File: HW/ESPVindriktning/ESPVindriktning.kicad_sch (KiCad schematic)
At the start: 60 parts, among them SW101 reset, SW102 boot, T101 BSS138, T102 BSS138, X101 USB_C, X102 I2C, X105 Fan, X106 PM1006, X107 I2C, X108 I2C

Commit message: Implement review findings
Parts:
- added C102: 1n, Capacitor_SMD:C_0603_1608Metric, symbol Device:C_Small
- added R103 (x2): 100R, Resistor_SMD:R_0603_1608Metric, symbol Device:R_Small
- C102: Partnumber 133-5641 -> (none); Supplier RS-Components -> (none)
- C221, C222, C224, C225, C501, C502, R101, R102, R103, R223: Supplier RS-Components -> (none)
- PD101: value PT26-51B/TR8 -> SFH 3716; footprint LED_SMD:LED_1210_3225Metric_Pad1.42x2.65mm_HandSolder -> LED_SMD:LED_0805_2012Metric_Pad1.15x1.40mm_HandSolder; Partnumber (none) -> 720-SFH3716; Supplier (none) -> Mouser
- R103: value 4.7k -> 470R; Partnumber 595-TLV76133DCYR -> (none); Supplier Mouser -> (none)
- X102: value I2C -> WS2812
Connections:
- net +3.3V: no longer C502.1, C502.1, C502.1, C502.1, D105.1 (VDD), D106.1 (VDD), D107.1 (VDD), X102.1 (Pin_1)
- net +5V: now also C502.1, C502.1, C502.1, C502.1, D105.1 (VDD), D106.1 (VDD), D107.1 (VDD), X102.1 (Pin_1)
- net BUZZER: now also S102.17 (GPIO1/ADC1_CH1/XTAL_32K_N); no longer S102.7 (GPIO8)
- net FAN: now also S102.18 (GPIO0/ADC1_CH0/XTAL_32K_P); no longer S102.6 (GPIO7)
- net GND: now also C102.2
- net GPIO0: now also R103.1; no longer D104.2 (A2), SW102.2
- net I2C_SCL: now also S102.6 (GPIO7); no longer S102.18 (GPIO0/ADC1_CH0/XTAL_32K_P)
- net I2C_SDA: now also S102.7 (GPIO8); no longer S102.17 (GPIO1/ADC1_CH1/XTAL_32K_N)
- net USB_D+: now also S102.14 (GPIO19/USB_D+); no longer S102.13 (GPIO18/USB_D-)
- net USB_D-: now also S102.13 (GPIO18/USB_D-); no longer S102.14 (GPIO19/USB_D+)
- net ~{RESET}: now also R103.1; no longer C102.1, D102.2 (A2), SW101.2
- new net: C102.1, D102.2 (A2), R103.2, SW101.2
- new net: C102.1, D104.2 (A2), R103.2, SW102.2
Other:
- moved on the sheet: C102, D102, D104, R103, SW101, SW102

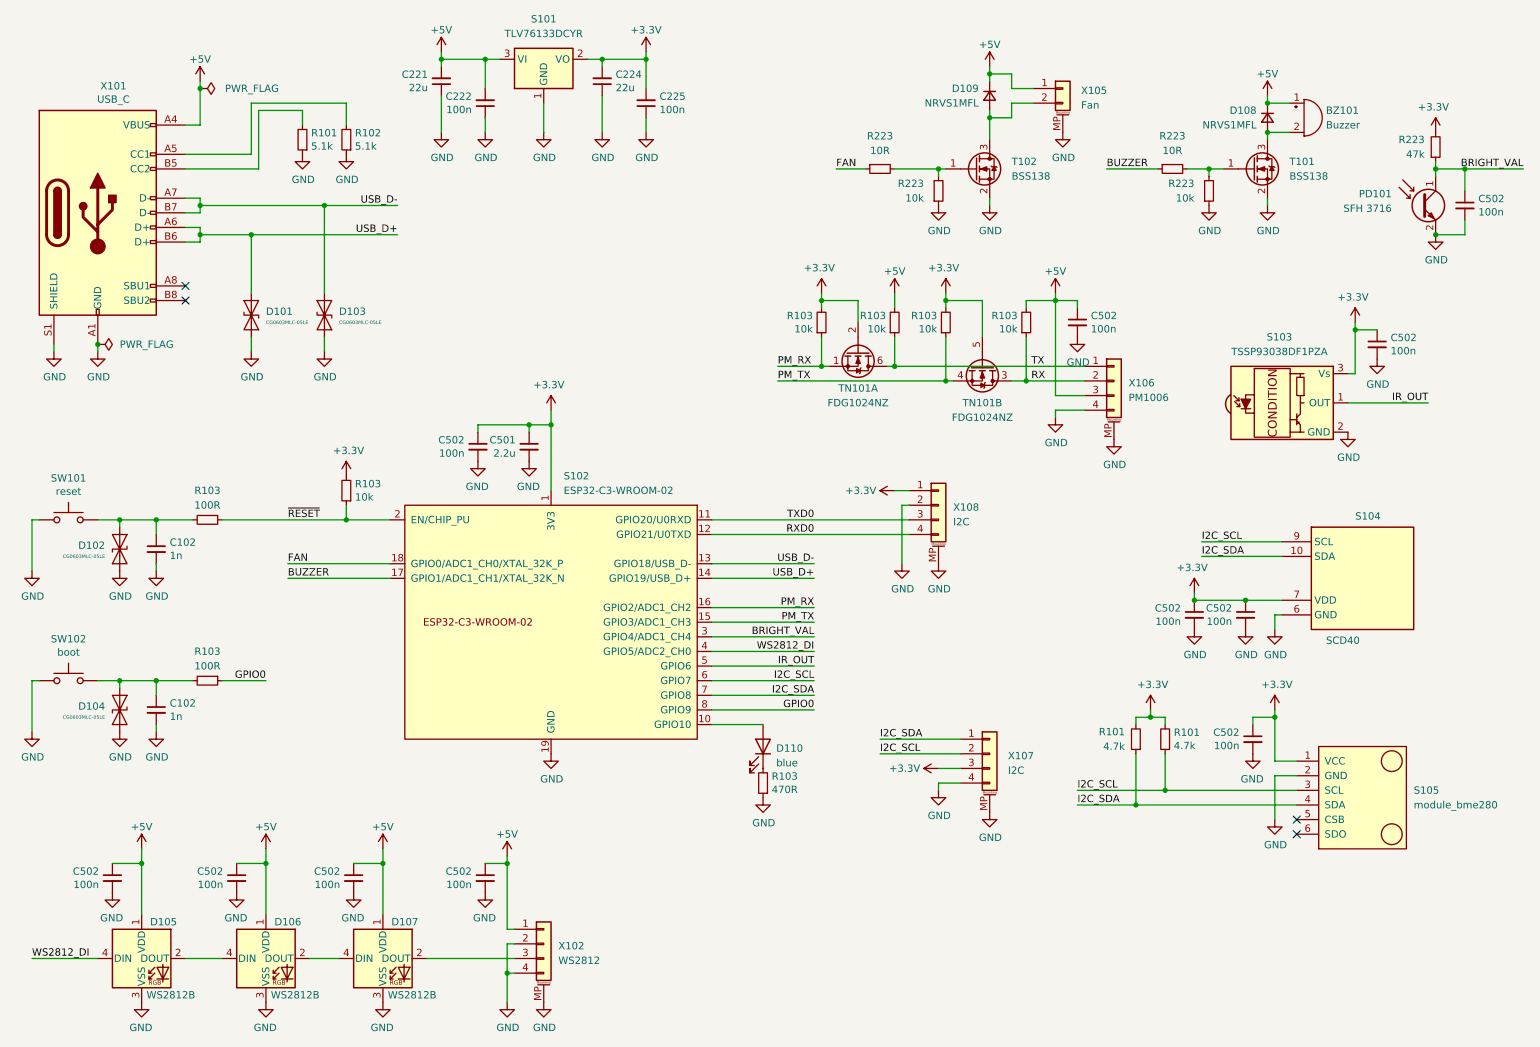
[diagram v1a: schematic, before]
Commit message: Review and layout optimization
Changes to schematic:
 - Add BME280 as ASIC under the module
 - Reduce I2C Pull-Ups to 1.2k

Changes to layout:
 - Optimize parts placement
 - Make USB approx. 9ß OHm impedance
 - General routing improvements
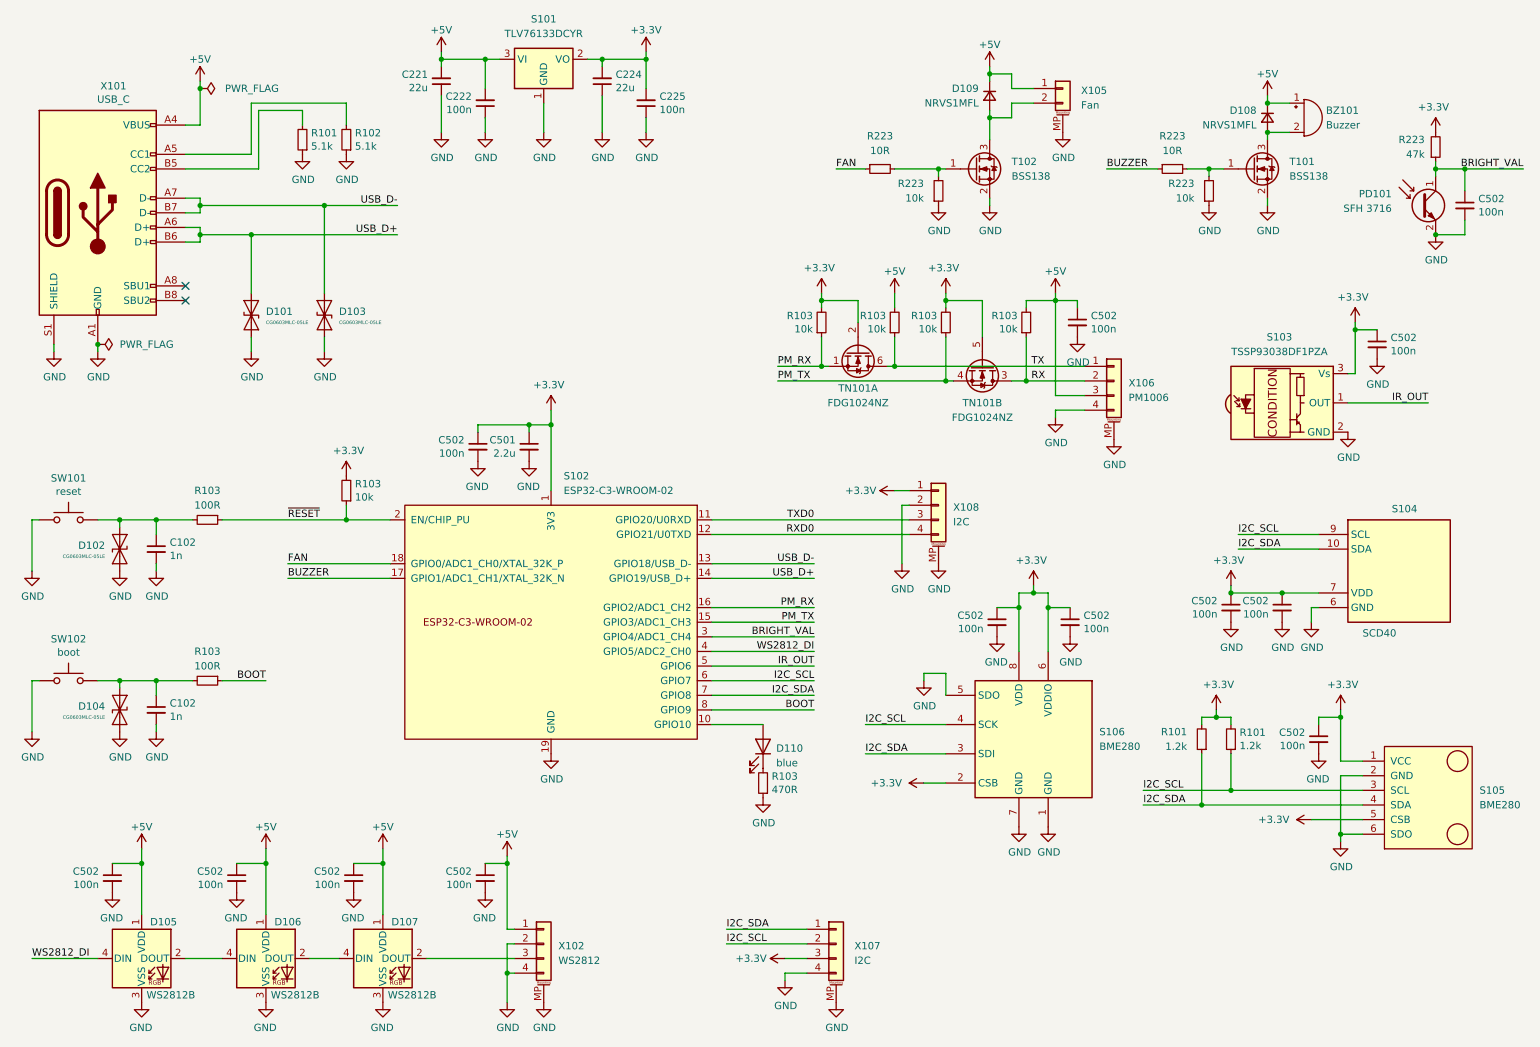
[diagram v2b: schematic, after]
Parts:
- added C502 (x2): 100n, Capacitor_SMD:C_0603_1608Metric, symbol Device:C_Small
- added S106: BME280, Package_LGA:Bosch_LGA-8_2.5x2.5mm_P0.65mm_ClockwisePinNumbering, symbol Sensor:BME280
- R101: value 4.7k -> 1.2k
- S105: value module_bme280 -> BME280
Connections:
- net +3.3V: now also S105.5 (CSB), C502.1, C502.1, S106.2 (CSB), S106.6 (VDDIO), S106.8 (VDD)
- net GND: now also S105.6 (SDO), C502.2, C502.2, S106.1 (GND), S106.5 (SDO), S106.7 (GND)
- net I2C_SCL: now also S106.4 (SCK)
- net I2C_SDA: now also S106.3 (SDI)
- net GPIO0 renamed BOOT
- no-connect marks 4 -> 2
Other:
- moved on the sheet: C502, R101, S104, S105, X107

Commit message: ESP32-C3 pinout change
Change pinout due to GPIO2 needing a Pull-Up (strapping pin)
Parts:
- added R103: 10k, Resistor_SMD:R_0603_1608Metric, symbol Device:R_Small
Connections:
- net +3.3V: now also R103.2
- net BRIGHT_VAL: now also S102.15 (GPIO3/ADC1_CH3); no longer S102.3 (GPIO4/ADC1_CH4)
- net PM_RX: now also S102.4 (GPIO5/ADC2_CH0); no longer S102.16 (GPIO2/ADC1_CH2)
- net PM_TX: now also S102.3 (GPIO4/ADC1_CH4); no longer S102.15 (GPIO3/ADC1_CH3)
- net WS2812_DI: now also S102.16 (GPIO2/ADC1_CH2), R103.1; no longer S102.4 (GPIO5/ADC2_CH0)
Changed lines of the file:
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@@
     (stroke (width 0) (type default))
   )
-  (wire (pts (xy 140.97 127) (xy 158.75 127))
+  (wire (pts (xy 140.97 119.38) (xy 162.56 119.38))
     (stroke (width 0) (type default))
   )
@@
     (stroke (width 0) (type default))
   )
-  (wire (pts (xy 140.97 119.38) (xy 158.75 119.38))
+  (wire (pts (xy 140.97 124.46) (xy 158.75 124.46))
     (stroke (width 0) (type default))
   )
@@
     (stroke (width 0) (type default))
   )
-  (wire (pts (xy 140.97 124.46) (xy 158.75 124.46))
+  (wire (pts (xy 140.97 121.92) (xy 158.75 121.92))
     (stroke (width 0) (type default))
   )
@@
     (stroke (width 0) (type default))
   )
+  (wire (pts (xy 162.56 118.11) (xy 162.56 119.38))
+    (stroke (width 0) (type default))
+  )
   (wire (pts (xy 101.6 24.13) (xy 101.6 29.21))
     (stroke (width 0) (type default))
@@
     (stroke (width 0) (type default))
   )
-  (wire (pts (xy 140.97 121.92) (xy 158.75 121.92))
+  (wire (pts (xy 140.97 127) (xy 158.75 127))
     (stroke (width 0) (type default))
   )
@@
     (effects (font (size 1.27 1.27)) (justify right bottom))
   )
-  (label "PM_RX" (at 158.75 119.38 180) (fields_autoplaced)
+  (label "PM_RX" (at 158.75 127 180) (fields_autoplaced)
     (effects (font (size 1.27 1.27)) (justify right bottom))
   )
@@
     (effects (font (size 1.27 1.27)) (justify left bottom))
   )
-  (label "WS2812_DI" (at 158.75 127 180) (fields_autoplaced)
+  (label "WS2812_DI" (at 158.75 119.38 180) (fields_autoplaced)
     (effects (font (size 1.27 1.27)) (justify right bottom))
   )
@@
     (effects (font (size 1.27 1.27)) (justify left bottom))
   )
-  (label "BRIGHT_VAL" (at 158.75 124.46 180) (fields_autoplaced)
+  (label "BRIGHT_VAL" (at 158.75 121.92 180) (fields_autoplaced)
     (effects (font (size 1.27 1.27)) (justify right bottom))
   )
-  (label "PM_TX" (at 158.75 121.92 180) (fields_autoplaced)
+  (label "PM_TX" (at 158.75 124.46 180) (fields_autoplaced)
     (effects (font (size 1.27 1.27)) (justify right bottom))
   )
@@
     )
   )
+  (symbol (lib_id "power:+3.3V") (at 162.56 113.03 0) (unit 1)
+    (in_bom yes) (on_board yes) (dnp no)
+    (property "Reference" "#PWR0613" (at 162.56 116.84 0)
+      (effects (font (size 1.27 1.27)) hide)
+    )
+    (property "Value" "+3.3V" (at 162.941 108.6358 0)
+      (effects (font (size 1.27 1.27)))
+    )
+    (property "Footprint" "" (at 162.56 113.03 0)
+      (effects (font (size 1.27 1.27)) hide)
+    )
+    (property "Datasheet" "" (at 162.56 113.03 0)
+      (effects (font (size 1.27 1.27)) hide)
+    )
+    (pin "1")
+    (instances
+      (project "musical-box"
+        (path "/4e262251-3bb5-4225-8327-98434df8b984"
+          (reference "#PWR0613") (unit 1)
+        )
+      )
+      (project "ESPVindriktning"
+        (path "/b0ce6775-8a27-40f1-94b2-96fe045c7efd"
+          (reference "#PWR0181") (unit 1)
+        )
+      )
+    )
+  )
   (symbol (lib_id "Device:C_Small") (at 121.92 27.94 0) (mirror x) (unit 1)
     (in_bom yes) (on_board yes) (dnp no)
@@
         )
       )
+    )
+  )
+  (symbol (lib_id "Device:R_Small") (at 162.56 115.57 180) (unit 1)
+    (in_bom yes) (on_board yes) (dnp no)
+    (property "Reference" "R103" (at 164.0586 114.4016 0)
+      (effects (font (size 1.27 1.27)) (justify right))
+    )
+    (property "Value" "10k" (at 164.0586 116.713 0)
+      (effects (font (size 1.27 1.27)) (justify right))
+    )
+    (property "Footprint" "Resistor_SMD:R_0603_1608Metric" (at 162.56 115.57 0)
+      (effects (font (size 1.27 1.27)) hide)
+    )
+    (property "Datasheet" "~" (at 162.56 115.57 0)
+      (effects (font (size 1.27 1.27)) hide)
+    )
+    (property "DNP" "" (at 162.56 115.57 0)
+      (effects (font (size 1.27 1.27)) hide)
+    )
+    (property "Partnumber" "" (at 162.56 115.57 0)
+      (effects (font (size 1.27 1.27)) hide)
+    )
+    (property "Supplier" "" (at 162.56 115.57 0)
+      (effects (font (size 1.27 1.27)) hide)
+    )
+    (pin "2")
+    (pin "1")
+    (instances
+      (project "musical-box"
+        (path "/4e262251-3bb5-4225-8327-98434df8b984"
+          (reference "R103") (unit 1)
+        )
+      )
+      (project "ESPVindriktning"
+        (path "/b0ce6775-8a27-40f1-94b2-96fe045c7efd"
+          (reference "R118") (unit 1)
+        )
+      )

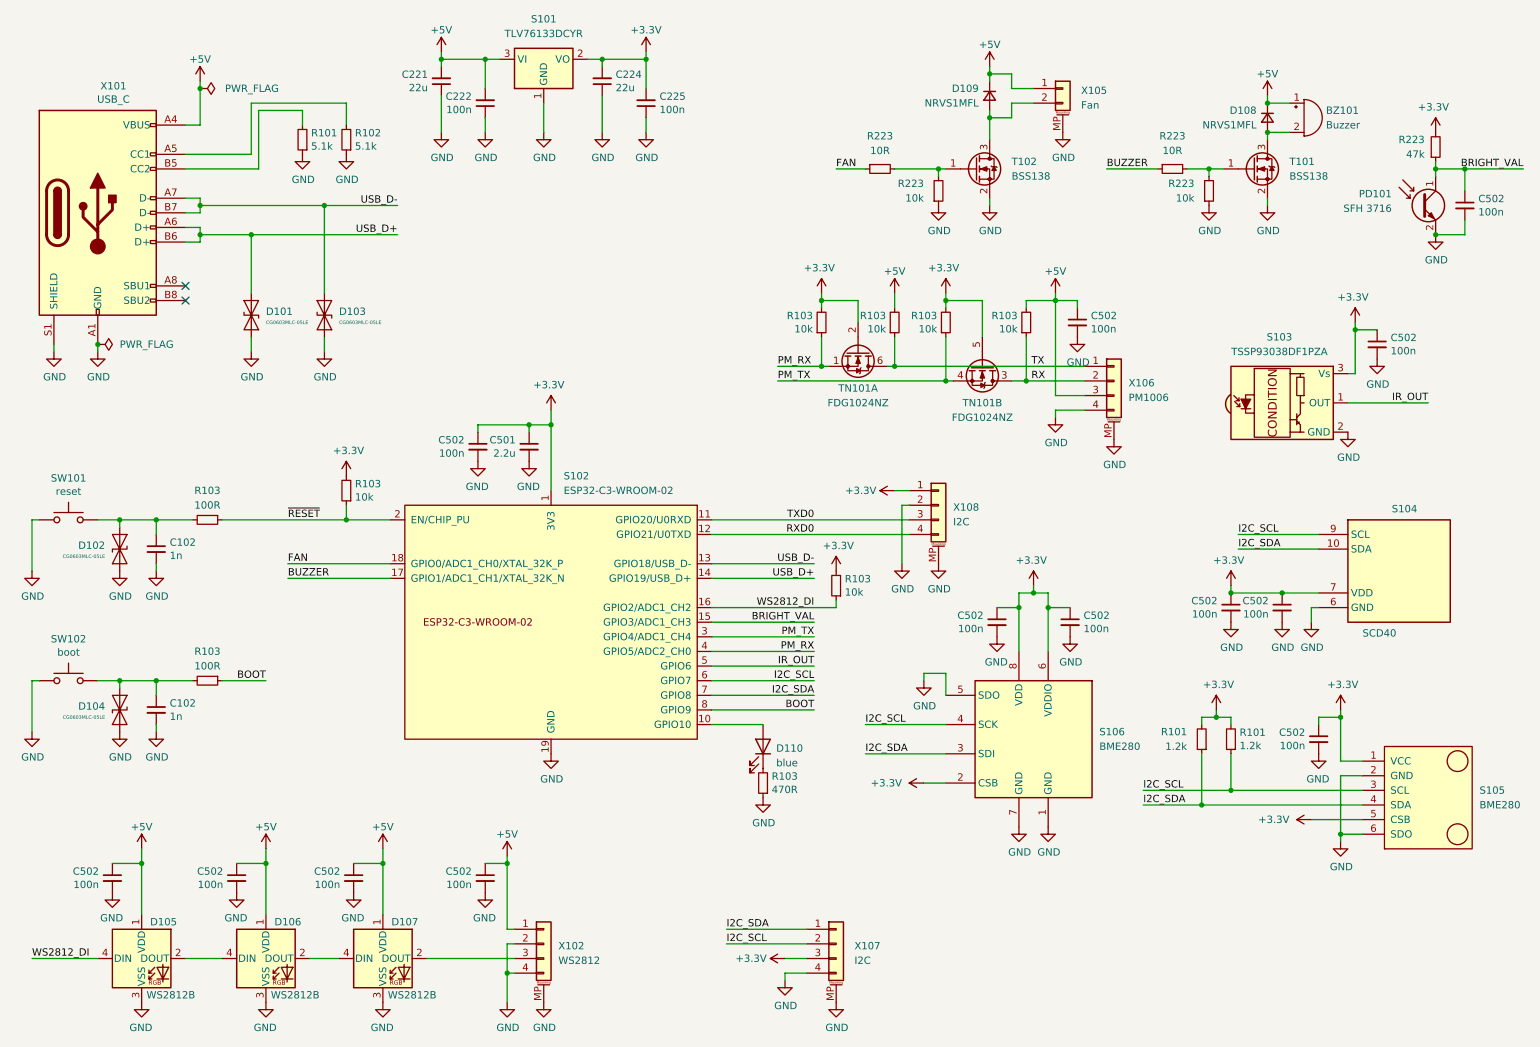
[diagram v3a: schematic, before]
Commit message: Add testpoints to schematic and layout
Implement improvements from Andreas (Breaker04)
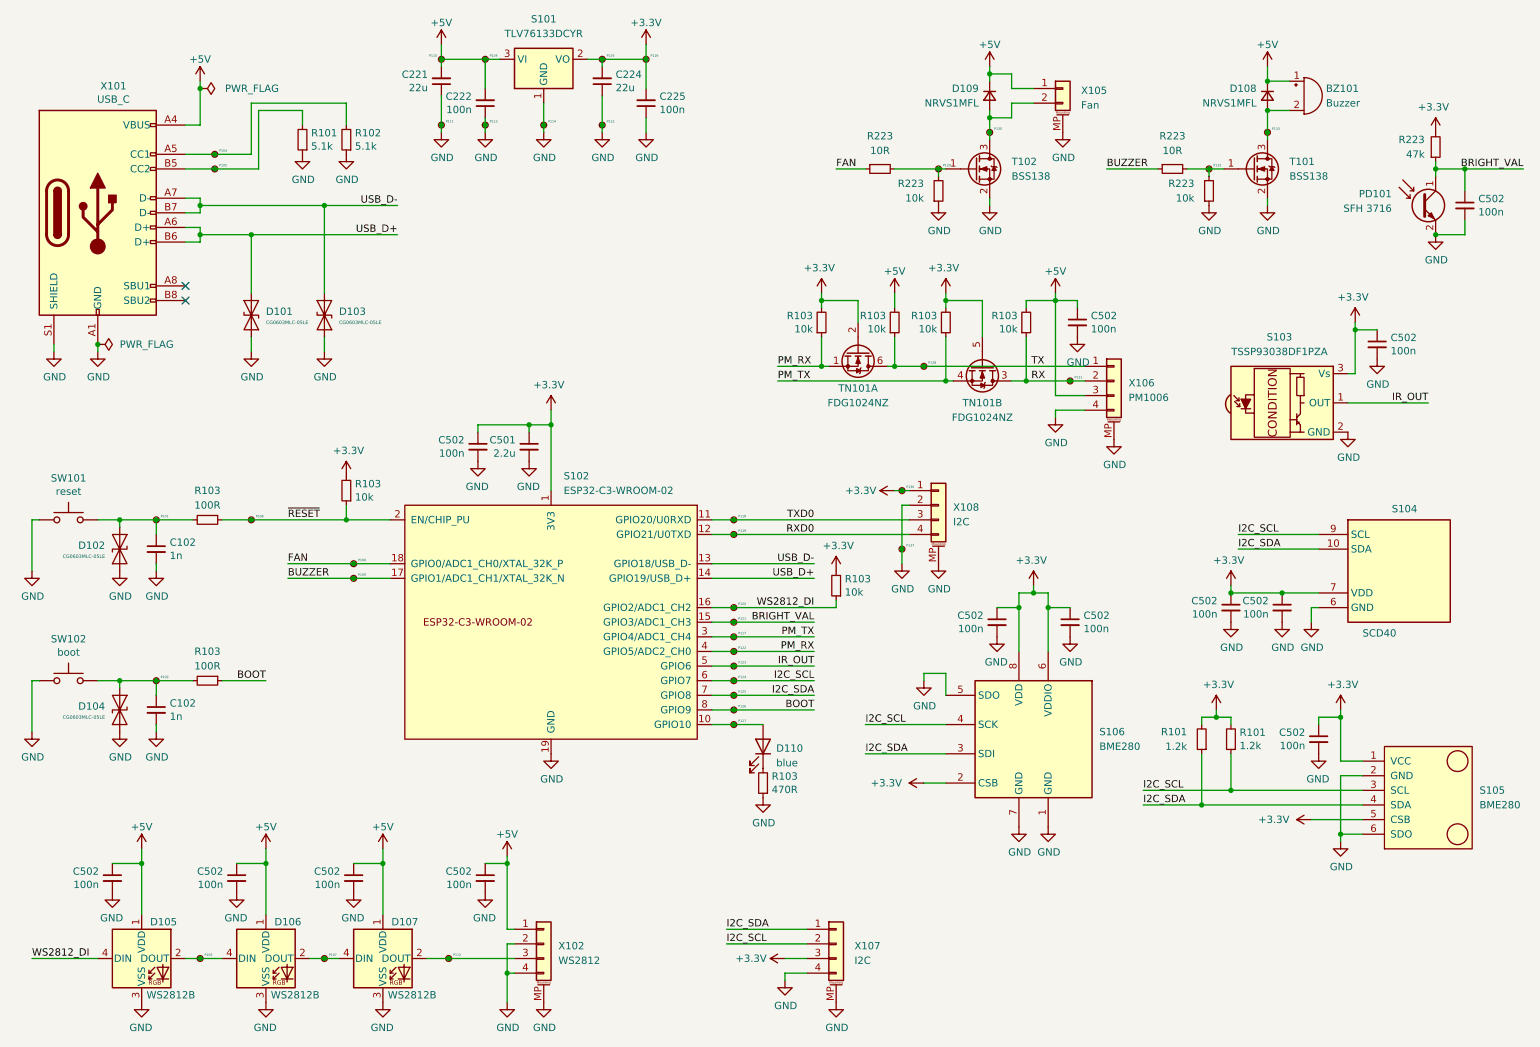
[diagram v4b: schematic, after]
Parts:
- added P101, P102, P103, P104, P105, P106, P107, P108, P109, P110, P111, P112, P113, P114, P115, P116, P117, P118, P119, P120, P121, P122, P123, P124, P125, P126, P127, P128, P129, P130, P131, P132, P133, P134, P135, P136, P137: TestPoint_Small, TestPoint:TestPoint_Pad_D1.0mm, symbol Connector:TestPoint_Small
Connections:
- net +3.3V: now also P116.1, P135.1, P136.1
- net +5V: now also P110.1, P134.1
- net BOOT: now also P126.1
- net BRIGHT_VAL: now also P121.1
- net BUZZER: now also P109.1
- net FAN: now also P108.1
- net GND: now also P111.1, P113.1, P114.1, P115.1, P137.1
- net I2C_SCL: now also P124.1
- net I2C_SDA: now also P125.1
- net IR_OUT: now also P123.1
- net PM_RX: now also P122.1
- net PM_TX: now also P117.1
- net RX: now also P131.1
- net RXD0: now also P119.1
- net TX: now also P128.1
- net TXD0: now also P118.1
- net WS2812_DI: now also P120.1
- net ~{RESET}: now also P106.1
- net at R223.2, R223.2, T101.1 (G): now also P132.1
- net at R102.2, X101.A5 (CC1): now also P104.1
- net at R101.2, X101.B5 (CC2): now also P105.1
- net at C102.1, D102.2 (A2), R103.2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: now also P101.1
- net at C102.1, D104.2 (A2), R103.2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: now also P102.1
- net at D109.2 (A), T102.3 (D), X105.2 (Pin_2): now also P130.1
- net at D107.2 (DOUT), X102.3 (Pin_3): now also P112.1
- net at R223.2, R223.2, T102.1 (G): now also P129.1
- net at BZ101.2 (+), D108.2 (A), T101.3 (D): now also P133.1
- net at D105.2 (DOUT), D106.4 (DIN): now also P103.1
- net at D106.2 (DOUT), D107.4 (DIN): now also P107.1
- net at D110.2 (A), S102.10 (GPIO10): now also P127.1
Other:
- moved on the sheet: BZ101, D108

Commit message: Add GND stitching, PCB production information and clean up silkscreen and fab layers
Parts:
- X108: value I2C -> UART
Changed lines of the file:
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@@
       (effects (font (size 1.27 1.27)) (justify left))
     )
-    (property "Value" "I2C" (at 182.88 104.4956 0)
+    (property "Value" "UART" (at 182.88 104.4956 0)
       (effects (font (size 1.27 1.27)) (justify left))
     )
